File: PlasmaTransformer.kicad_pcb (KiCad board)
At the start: 2 copper layers, 90 x 90 mm, 74 parts, among them J1 Barrel_Jack_MountingPin, J11 Screw_Terminal_01x01, J12 Screw_Terminal_01x01, J2 Conn_01x02_Pin, J3 Conn_Coaxial, J4 Conn_02x04_Odd_Even, J5 Conn_Coaxial, J6 Conn_01x02_Pin, J7 Conn_01x02_Pin, J8 AudioJack3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

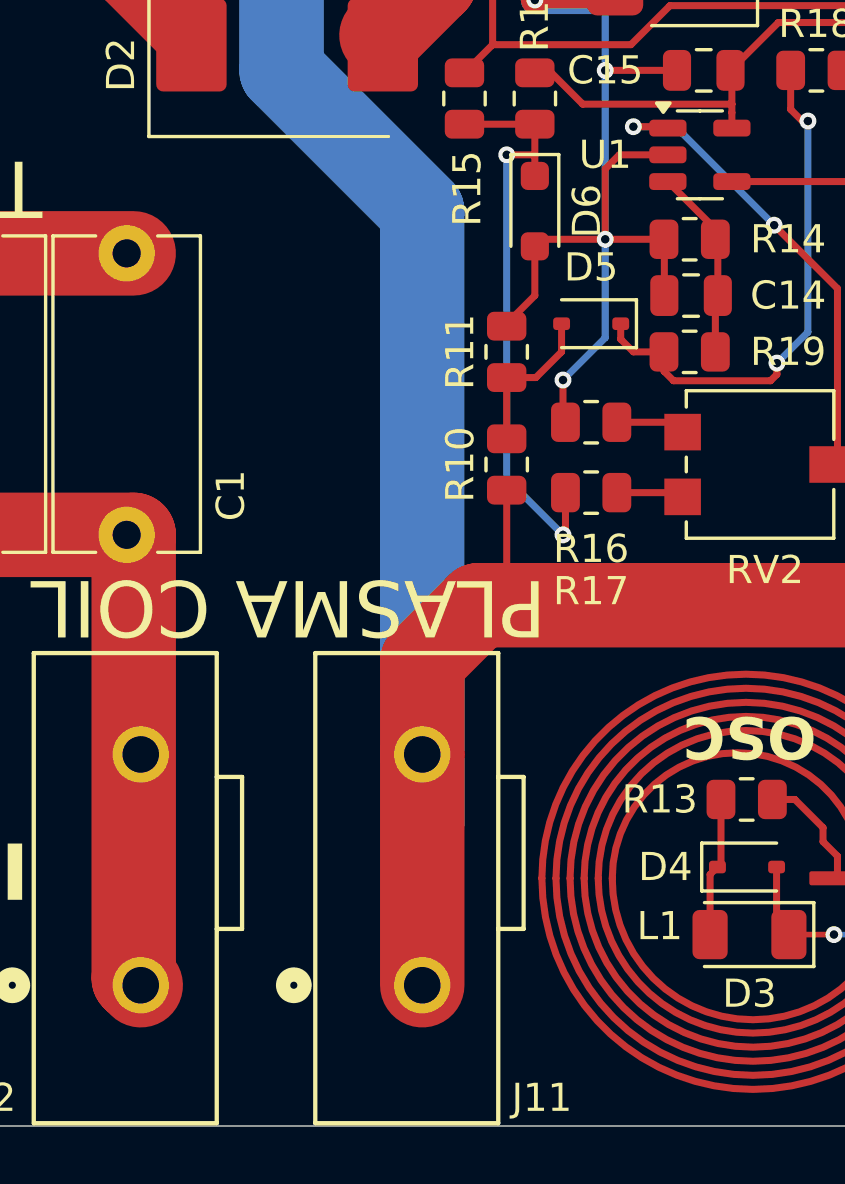
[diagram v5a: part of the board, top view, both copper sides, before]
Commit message: Design cleanup, part selection and BOM update
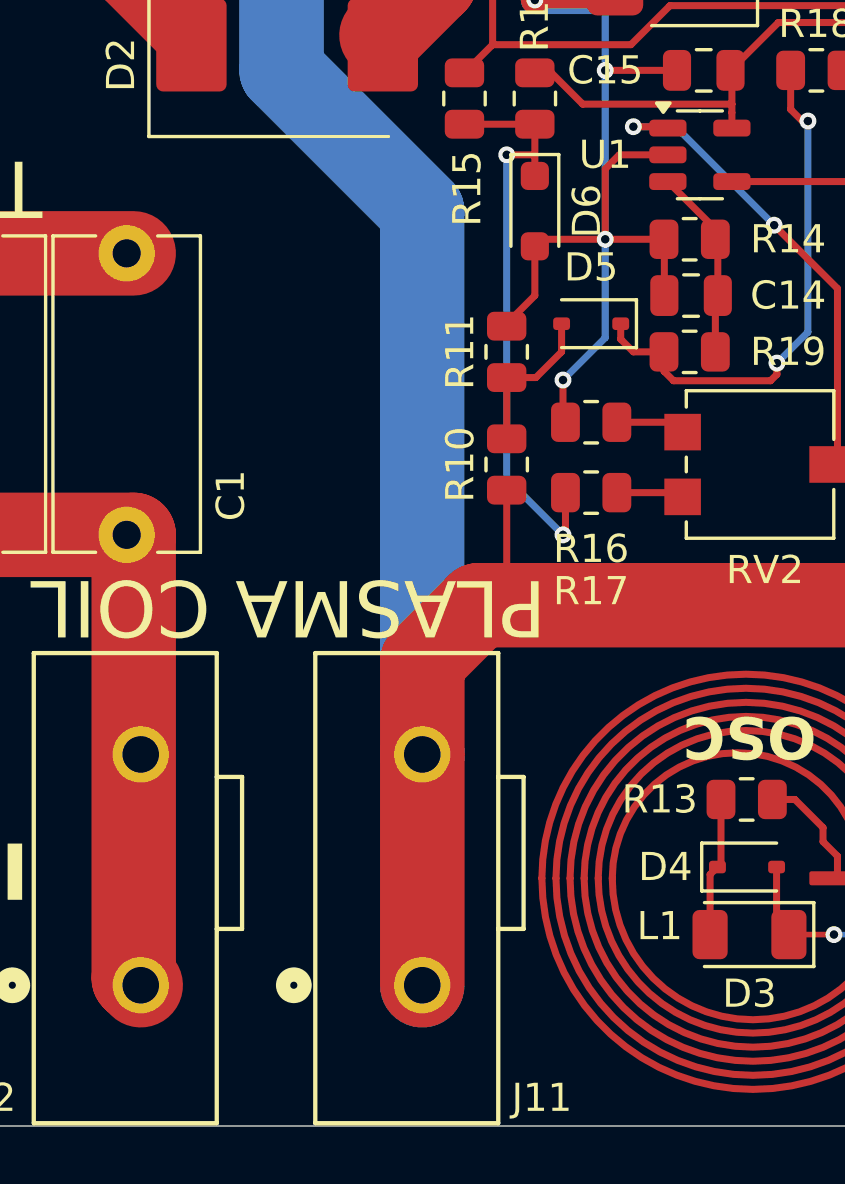
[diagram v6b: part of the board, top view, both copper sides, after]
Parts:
- R7, R8: value 49.9 -> 499
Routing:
- net /DRAIN: track 165.5 -> 171.2 mm
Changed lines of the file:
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@@
 			(psa4output no)
 			(plot_black_and_white yes)
-			(plotinvisibletext no)
 			(sketchpadsonfab no)
 			(plotpadnumbers no)
@@
 			)
 		)
+		(property "MPN" "ESQ-102-33-G-S"
+			(at 0 0 0)
+			(unlocked yes)
+			(layer "F.Fab")
+			(hide yes)
+			(effects
+				(font
+					(size 1 1)
+					(thickness 0.15)
+				)
+			)
+		)
+		(property "Manufacturer" "Samtec"
+			(at 0 0 0)
+			(unlocked yes)
+			(layer "F.Fab")
+			(hide yes)
+			(effects
+				(font
+					(size 1 1)
+					(thickness 0.15)
+				)
+			)
+		)
 		(property ki_fp_filters "Connector*:*_1x??_*")
 		(sheetname "/")
@@
 			)
 		)
+		(property "MPN" "CRA2512-FZ-R050ELF"
+			(at 0 0 270)
+			(unlocked yes)
+			(layer "F.Fab")
+			(hide yes)
+			(effects
+				(font
+					(size 1 1)
+					(thickness 0.15)
+				)
+			)
+		)
+		(property "Manufacturer" "Bourns"
+			(at 0 0 270)
+			(unlocked yes)
+			(layer "F.Fab")
+			(hide yes)
+			(effects
+				(font
+					(size 1 1)
+					(thickness 0.15)
+				)
+			)
+		)
 		(property ki_fp_filters "R_*")
 		(sheetname "/")
@@
 			)
 		)
-		(property "Manufacturer" ""
+		(property "Manufacturer" "Samsung"
 			(at 0 0 0)
 			(unlocked yes)
@@
 			)
 		)
-		(property "MPN" ""
+		(property "MPN" "CL21B104KCFNNNE"
 			(at 0 0 0)
 			(unlocked yes)
@@
 			)
 		)
-		(property "MPN" ""
+		(property "MPN" "RC0805FR-1322KL"
 			(at 0 0 0)
 			(unlocked yes)
@@
 			)
 		)
-		(property "Manufacturer" ""
+		(property "Manufacturer" "Yageo"
 			(at 0 0 0)
 			(unlocked yes)
@@
 			)
 		)
-		(property "MPN" ""
+		(property "MPN" "RC0805FR-134K7L"
 			(at 0 0 0)
 			(unlocked yes)
@@
 			)
 		)
-		(property "MPN" ""
+		(property "MPN" "RC0805FR-134K7L"
 			(at 0 0 270)
 			(unlocked yes)
@@
 			)
 		)
-		(property "MPN" ""
+		(property "MPN" "RC0805JR-070RL"
 			(at 0 0 0)
 			(unlocked yes)
@@
 			)
 		)
-		(property "Manufacturer" ""
+		(property "Manufacturer" "Yageo"
 			(at 0 0 0)
 			(unlocked yes)
@@
 			)
 		)
-		(property "MPN" ""
+		(property "MPN" "RC0805JR-070RL"
 			(at 0 0 180)
 			(unlocked yes)
@@
 			)
 		)
-		(property "Manufacturer" ""
+		(property "Manufacturer" "Yageo"
 			(at 0 0 180)
 			(unlocked yes)
@@
 			)
 		)
-		(property "MPN" ""
+		(property "MPN" "RC0805FR-1322KL"
 			(at 0 0 90)
 			(unlocked yes)
@@
 			)
 		)
-		(property "Manufacturer" ""
+		(property "Manufacturer" "Yageo"
 			(at 0 0 90)
 			(unlocked yes)
@@
 			)
 		)
+		(property "MPN" "LM397MF/NOPB"
+			(at 0 0 0)
+			(unlocked yes)
+			(layer "F.Fab")
+			(hide yes)
+			(effects
+				(font
+					(size 1 1)
+					(thickness 0.15)
+				)
+			)
+		)
+		(property "Manufacturer" "TI"
+			(at 0 0 0)
+			(unlocked yes)
+			(layer "F.Fab")
+			(hide yes)
+			(effects
+				(font
+					(size 1 1)
+					(thickness 0.15)
+				)
+			)
+		)
 		(property ki_fp_filters "SOT?23*")
 		(sheetname "/")
@@
 			)
 		)
-		(property "MPN" ""
+		(property "MPN" "RC0805FR-1322KL"
 			(at 0 0 0)
 			(unlocked yes)
@@
 			)
 		)
-		(property "Manufacturer" ""
+		(property "Manufacturer" "Yageo"
 			(at 0 0 0)
 			(unlocked yes)
@@
 			)
 		)
-		(property "Manufacturer" ""
+		(property "Manufacturer" "Murata"
 			(at 0 0 180)
 			(unlocked yes)
@@
 			)
 		)
-		(property "MPN" ""
+		(property "MPN" "GRM43DR7LW104KW01K"
 			(at 0 0 180)
 			(unlocked yes)
@@
 			)
 		)
+		(property "MPN" "ESQ-102-33-G-S"
+			(at 0 0 0)
+			(unlocked yes)
+			(layer "F.Fab")
+			(hide yes)
+			(effects
+				(font
+					(size 1 1)
+					(thickness 0.15)
+				)
+			)
+		)
+		(property "Manufacturer" "Samtec"
+			(at 0 0 0)
+			(unlocked yes)
+			(layer "F.Fab")
+			(hide yes)
+			(effects
+				(font
+					(size 1 1)
+					(thickness 0.15)
+				)
+			)
+		)
 		(property ki_fp_filters "Connector*:*_1x??_*")
 		(sheetname "/")
@@
 			)
 		)
-		(property "Value" "49.9"
+		(property "Value" "499"
 			(at 0 2.28 180)
 			(layer "F.Fab")
@@
 			)
 		)
-		(property "MPN" "RC2010FK-0749R9L"
+		(property "MPN" "RC2010FK-07499RL"
 			(at 0 0 180)
 			(unlocked yes)
@@
 			)
 		)
+		(property "MPN" "BUK9832-55A/CUX"
+			(at 0 0 0)
+			(unlocked yes)
+			(layer "F.Fab")
+			(hide yes)
+			(effects
+				(font
+					(size 1 1)
+					(thickness 0.15)
+				)
+			)
+		)
+		(property "Manufacturer" "Nexperia"
+			(at 0 0 0)
+			(unlocked yes)
+			(layer "F.Fab")
+			(hide yes)
+			(effects
+				(font
+					(size 1 1)
+					(thickness 0.15)
+				)
+			)
+		)
 		(property ki_fp_filters "SOT?223*")
 		(sheetname "/")
@@
 			)
 		)
-		(property "Value" "49.9"
+		(property "Value" "499"
 			(at 0 2.28 180)
 			(layer "F.Fab")
@@
 			)
 		)
-		(property "MPN" "RC2010FK-0749R9L"
+		(property "MPN" "RC2010FK-07499RL"
 			(at 0 0 180)
 			(unlocked yes)
@@
 			)
 		)
-		(property "Manufacturer" ""
+		(property "Manufacturer" "Murata"
 			(at 0 0 0)
 			(unlocked yes)
@@
 			)
 		)
-		(property "MPN" ""
+		(property "MPN" "GRM21BR61E226ME44L"
 			(at 0 0 0)
 			(unlocked yes)
@@
 	)
 	(segment
-		(start 91.71 92)
-		(end 68.5 92)
-		(width 1)
+		(start 100 107.5)
+		(end 100 100.29)
+		(width 3)
 		(layer "B.Cu")
 		(net 36)
 	)
 	(segment
-		(start 105 134.300001)
-		(end 105 112.5)
-		(width 3)
+		(start 91.71 92)
+		(end 68.5 92)
+		(width 1)
 		(layer "B.Cu")
 		(net 36)
@@
 	)
 	(segment
-		(start 100 107.5)
-		(end 100 100.29)
+		(start 105 140)
+		(end 105 112.5)
 		(width 3)
 		(layer "B.Cu")
